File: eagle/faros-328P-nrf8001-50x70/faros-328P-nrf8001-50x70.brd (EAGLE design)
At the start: 49.2 x 69.8 mm, 13 parts, among them IC1 ATMEGA328P-PU

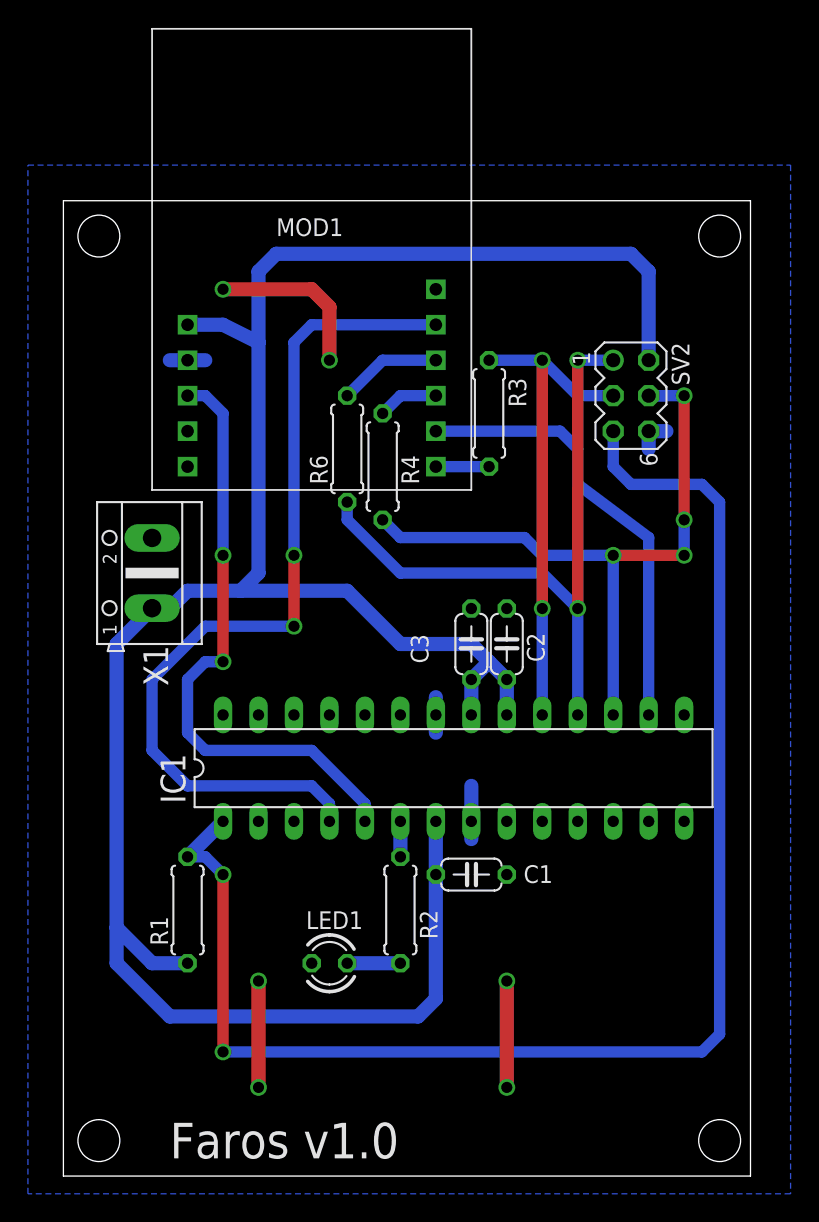
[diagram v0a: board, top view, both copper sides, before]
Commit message: Increased min. restring sizes and improved clearance
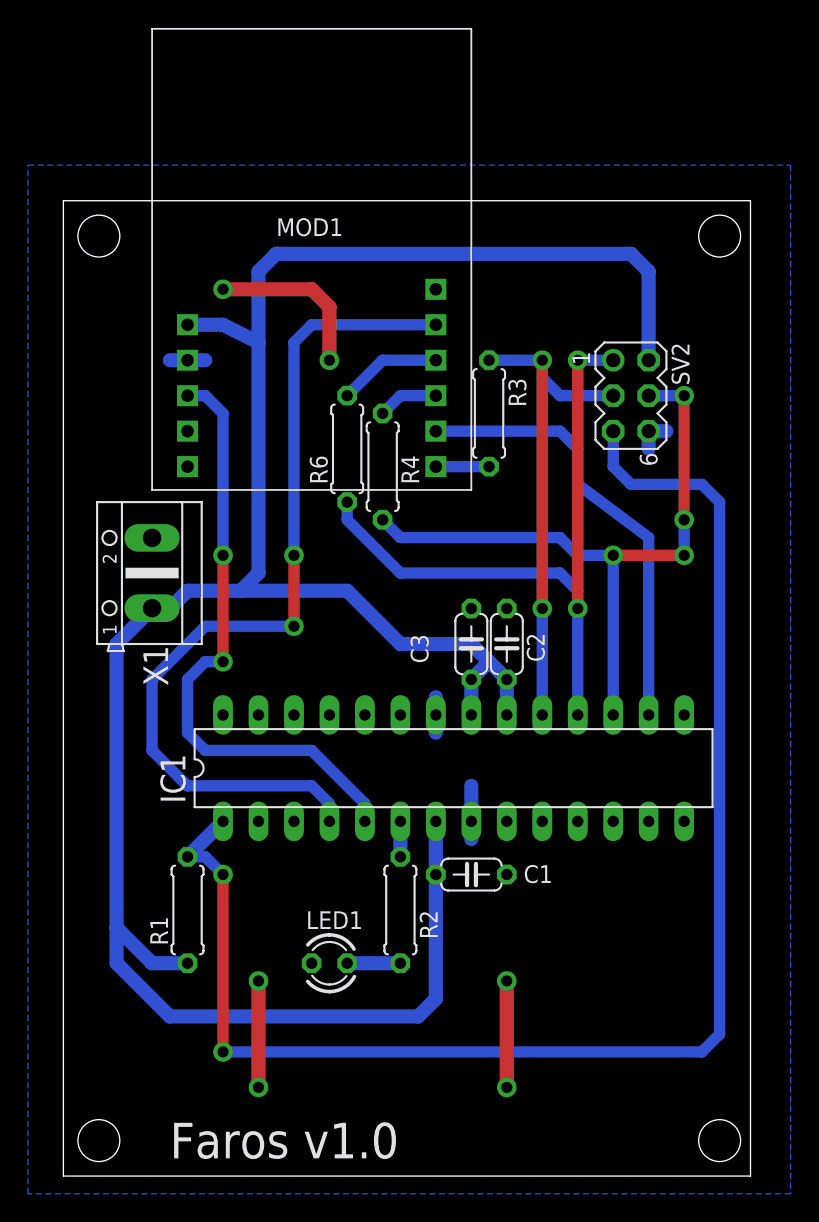
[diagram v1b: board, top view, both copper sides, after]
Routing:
- net N$2: track 35.3 -> 36.1 mm
- net N$14: track 48.4 -> 49.1 mm
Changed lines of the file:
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@@
 <param name="rvMicroViaOuter" value="0.25"/>
 <param name="rvMicroViaInner" value="0.25"/>
-<param name="rlMinPadTop" value="10mil"/>
+<param name="rlMinPadTop" value="12mil"/>
 <param name="rlMaxPadTop" value="20mil"/>
 <param name="rlMinPadInner" value="10mil"/>
 <param name="rlMaxPadInner" value="20mil"/>
-<param name="rlMinPadBottom" value="10mil"/>
+<param name="rlMinPadBottom" value="12mil"/>
 <param name="rlMaxPadBottom" value="20mil"/>
-<param name="rlMinViaOuter" value="8mil"/>
+<param name="rlMinViaOuter" value="12mil"/>
 <param name="rlMaxViaOuter" value="20mil"/>
-<param name="rlMinViaInner" value="8mil"/>
+<param name="rlMinViaInner" value="12mil"/>
 <param name="rlMaxViaInner" value="20mil"/>
 <param name="rlMinMicroViaOuter" value="4mil"/>
@@
 <wire x1="20.32" y1="48.26" x2="20.32" y2="46.99" width="0.8128" layer="16"/>
 <wire x1="20.32" y1="46.99" x2="24.13" y2="43.18" width="0.8128" layer="16"/>
-<wire x1="24.13" y1="43.18" x2="34.29" y2="43.18" width="0.8128" layer="16"/>
+<wire x1="24.13" y1="43.18" x2="35.56" y2="43.18" width="0.8128" layer="16"/>
 <wire x1="36.83" y1="33.02" x2="36.83" y2="40.64" width="0.8128" layer="16"/>
-<wire x1="36.83" y1="40.64" x2="34.29" y2="43.18" width="0.8128" layer="16"/>
 <via x="36.83" y="40.64" extent="1-16" drill="0.8" shape="square"/>
 <via x="36.83" y="58.42" extent="1-16" drill="0.8" shape="square"/>
 <wire x1="36.83" y1="58.42" x2="36.83" y2="40.64" width="0.8128" layer="1"/>
 <wire x1="36.83" y1="58.42" x2="39.37" y2="58.42" width="0.8128" layer="16"/>
+<wire x1="36.83" y1="40.64" x2="36.83" y2="41.91" width="0.8128" layer="16"/>
+<wire x1="36.83" y1="41.91" x2="35.56" y2="43.18" width="0.8128" layer="16"/>
 </signal>
 <signal name="N$19">
@@
 <wire x1="41.91" y1="55.88" x2="44.45" y2="55.88" width="0.8128" layer="16"/>
 <wire x1="39.37" y1="33.02" x2="39.37" y2="44.45" width="0.8128" layer="16"/>
-<wire x1="39.37" y1="44.45" x2="34.29" y2="44.45" width="0.8128" layer="16"/>
-<wire x1="34.29" y1="44.45" x2="33.02" y2="45.72" width="0.8128" layer="16"/>
-<wire x1="33.02" y1="45.72" x2="24.13" y2="45.72" width="0.8128" layer="16"/>
+<wire x1="35.56" y1="45.72" x2="24.13" y2="45.72" width="0.8128" layer="16"/>
 <wire x1="24.13" y1="45.72" x2="22.86" y2="46.99" width="0.8128" layer="16"/>
 <wire x1="44.45" y1="55.88" x2="44.45" y2="46.99" width="0.8128" layer="1"/>
+<wire x1="39.37" y1="44.45" x2="36.83" y2="44.45" width="0.8128" layer="16"/>
+<wire x1="36.83" y1="44.45" x2="35.56" y2="45.72" width="0.8128" layer="16"/>
 </signal>
 <signal name="N$2">
@@
 <contactref element="SV2" pad="3"/>
 <contactref element="R3" pad="1"/>
-<wire x1="39.37" y1="55.88" x2="36.83" y2="55.88" width="0.8128" layer="16"/>
-<wire x1="36.83" y1="55.88" x2="34.29" y2="58.42" width="0.8128" layer="16"/>
+<wire x1="39.37" y1="55.88" x2="35.56" y2="55.88" width="0.8128" layer="16"/>
 <wire x1="34.29" y1="58.42" x2="30.48" y2="58.42" width="0.8128" layer="16"/>
 <via x="34.29" y="40.64" extent="1-16" drill="0.8" shape="square"/>
 <wire x1="34.29" y1="33.02" x2="34.29" y2="40.64" width="0.8128" layer="16"/>
 <wire x1="34.29" y1="58.42" x2="34.29" y2="40.64" width="0.8128" layer="1"/>
+<wire x1="35.56" y1="55.88" x2="34.29" y2="57.15" width="0.8128" layer="16"/>
+<wire x1="34.29" y1="57.15" x2="34.29" y2="58.42" width="0.8128" layer="16"/>
 </signal>
 <signal name="N$6">

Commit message: Cleaned up part names. Added BOM to readme. Added PDF showing part placement for single-sided board. Updated Gerber files and PCB layout (PDF).
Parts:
- renumbered R6 to R5, SV2 to SV1
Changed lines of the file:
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@@
 <hole x="46.99" y="67.31" drill="3"/>
 <hole x="46.99" y="2.54" drill="3"/>
-<circle x="2.54" y="2.54" radius="3.5" width="0" layer="42"/>
-<circle x="46.99" y="2.54" radius="3.5" width="0" layer="42"/>
-<circle x="2.54" y="67.31" radius="3.5" width="0" layer="42"/>
-<circle x="46.99" y="67.31" radius="3.5" width="0" layer="42"/>
 <text x="7.62" y="1.27" size="2.54" layer="21">Faros v1.0</text>
 </plain>
@@
 <attribute name="VALUE" x="23.5712" y="21.336" size="1.27" layer="27" ratio="10" rot="R270"/>
 </element>
-<element name="SV2" library="con-lstb" package="MA03-2" value="" x="40.64" y="55.88" smashed="yes" rot="R270">
+<element name="SV1" library="con-lstb" package="MA03-2" value="" x="40.64" y="55.88" smashed="yes" rot="R270">
 <attribute name="OC_NEWARK" value="unknown" x="40.64" y="55.88" size="1.778" layer="27" rot="R270" display="off"/>
 <attribute name="MPN" value="" x="40.64" y="55.88" size="1.778" layer="27" rot="R270" display="off"/>
@@
 <attribute name="VALUE" x="23.4188" y="48.514" size="1.27" layer="27" ratio="10" rot="R90"/>
 </element>
-<element name="R6" library="rcl" package="0207/7" value="4.7 k" x="20.32" y="52.07" rot="R90"/>
+<element name="R5" library="rcl" package="0207/7" value="4.7 k" x="20.32" y="52.07" rot="R90"/>
 </elements>
 <signals>
@@
 <vertex x="-2.54" y="-1.27"/>
 </polygon>
-<contactref element="SV2" pad="6"/>
+<contactref element="SV1" pad="6"/>
 <via x="13.97" y="6.35" extent="1-16" drill="0.8" shape="square"/>
 <via x="31.75" y="6.35" extent="1-16" drill="0.8" shape="square"/>
@@
 <wire x1="13.97" y1="59.69" x2="11.43" y2="60.96" width="1.016" layer="16"/>
 <wire x1="11.43" y1="60.96" x2="8.89" y2="60.96" width="1.016" layer="16"/>
-<contactref element="SV2" pad="2"/>
+<contactref element="SV1" pad="2"/>
 <wire x1="41.91" y1="58.42" x2="41.91" y2="64.77" width="1.016" layer="16"/>
 <wire x1="41.91" y1="64.77" x2="40.64" y2="66.04" width="1.016" layer="16"/>
@@
 <contactref element="R1" pad="2"/>
 <wire x1="8.89" y1="22.86" x2="11.43" y2="25.4" width="1.016" layer="16"/>
-<contactref element="SV2" pad="5"/>
+<contactref element="SV1" pad="5"/>
 <wire x1="39.37" y1="53.34" x2="39.37" y2="50.8" width="0.8128" layer="16"/>
 <wire x1="39.37" y1="50.8" x2="40.64" y2="49.53" width="0.8128" layer="16"/>
@@
 <signal name="N$5">
 <contactref element="MOD1" pad="MISO"/>
-<contactref element="R6" pad="2"/>
+<contactref element="R5" pad="2"/>
 <wire x1="20.32" y1="55.88" x2="22.86" y2="58.42" width="0.8128" layer="16"/>
 <wire x1="22.86" y1="58.42" x2="26.67" y2="58.42" width="0.8128" layer="16"/>
@@
 <signal name="N$14">
 <contactref element="IC1" pad="18"/>
-<contactref element="SV2" pad="1"/>
-<contactref element="R6" pad="1"/>
+<contactref element="SV1" pad="1"/>
+<contactref element="R5" pad="1"/>
 <wire x1="20.32" y1="48.26" x2="20.32" y2="46.99" width="0.8128" layer="16"/>
 <wire x1="20.32" y1="46.99" x2="24.13" y2="43.18" width="0.8128" layer="16"/>
@@
 <signal name="N$19">
 <via x="44.45" y="55.88" extent="1-16" drill="0.8" shape="square"/>
-<contactref element="SV2" pad="4"/>
+<contactref element="SV1" pad="4"/>
 <contactref element="IC1" pad="17"/>
 <contactref element="R4" pad="1"/>
@@
 <via x="34.29" y="58.42" extent="1-16" drill="0.8" shape="square"/>
 <contactref element="IC1" pad="19"/>
-<contactref element="SV2" pad="3"/>
+<contactref element="SV1" pad="3"/>
 <contactref element="R3" pad="1"/>
 <wire x1="39.37" y1="55.88" x2="35.56" y2="55.88" width="0.8128" layer="16"/>
